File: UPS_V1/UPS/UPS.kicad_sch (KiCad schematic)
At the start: 77 parts, among them J1 Conn_01x02_Pin, J2 Conn_01x02_Pin, J3 USB_B_Micro, J4 Conn_01x02_Socket, J5 Conn_01x02_Pin, J6 Conn_01x02_Socket, U1 MT3608, U2 BQ24040DSQR, U3 LM2903, U4 TPS22810DRV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

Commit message: pcb layout
minor schematic adjustment and pcb layout
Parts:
- removed unit 2 of U3
- added H1, H2, H3, H4: MountingHole, MountingHole:MountingHole_3.2mm_M3, symbol Mechanical:MountingHole
- added J7: Conn_01x02_Pin, Connector_PinHeader_2.54mm:PinHeader_1x02_P2.54mm_Vertical, symbol Connector:Conn_01x02_Pin
- added J8, J9: Screw_Terminal_01x02, TerminalBlock:TerminalBlock_Xinya_XY308-2.54-2P_1x02_P2.54mm_Horizontal, symbol Connector:Screw_Terminal_01x02
- J1: footprint (none) -> Connector_PinHeader_2.54mm:PinHeader_1x02_P2.54mm_Vertical
- RV1: footprint footprints:3296W-1-103_BRN -> 3296W:3296W-1-103_BRN
- U2: footprint DSQ10_P9X1P5 -> BQ24040DSQR:DSQ10_P9X1P5
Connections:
- net 3.3VOUT: now also J8.1 (Pin_1)
- net 5VOUT: now also J9.1 (Pin_1)
- net GND: now also J7.1 (Pin_1), J8.2 (Pin_2), J9.2 (Pin_2)
- net at R8.2, U3.1, U4.5 (EN/UVLO): now also J7.2 (Pin_2)
- no-connect marks 6 -> 3

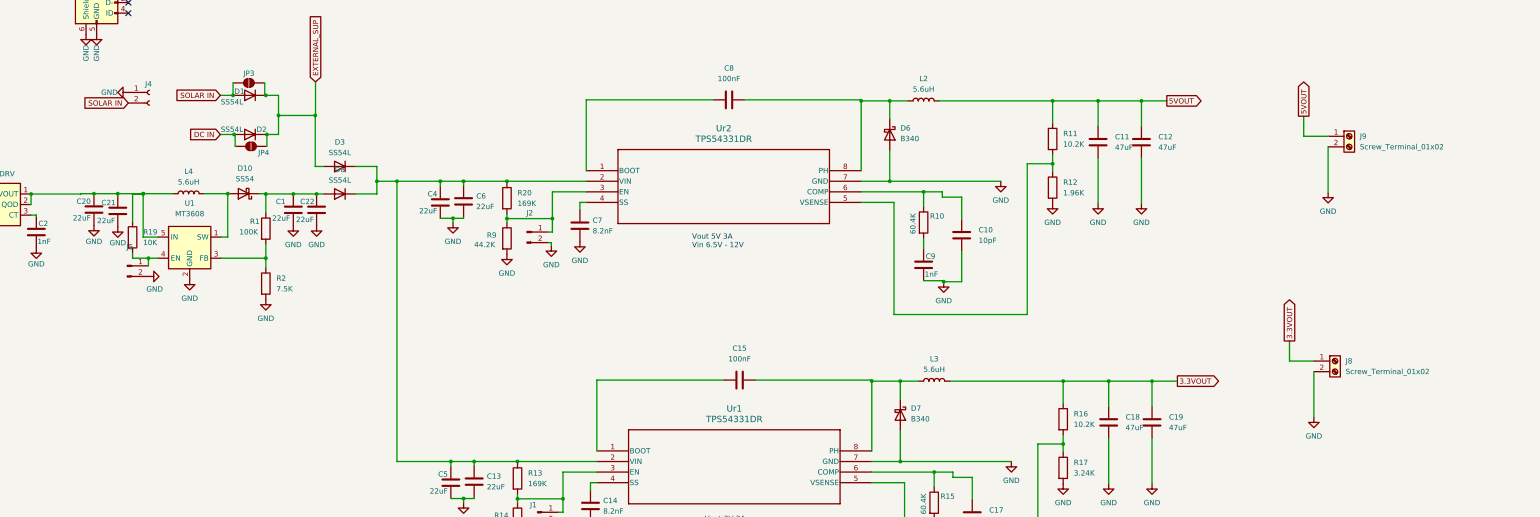
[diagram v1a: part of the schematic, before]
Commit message: added 1x12 terminal block
 1x12 terminal block
3d
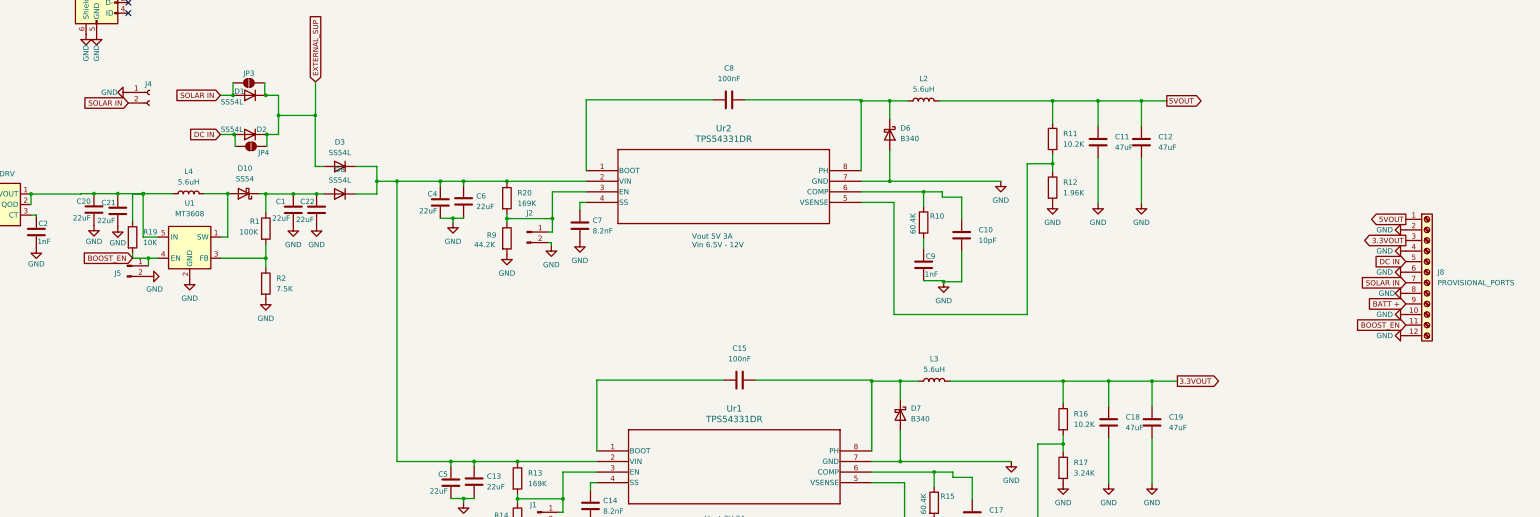
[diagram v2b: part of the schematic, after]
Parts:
- removed J8, J9: Screw_Terminal_01x02, TerminalBlock:TerminalBlock_Xinya_XY308-2.54-2P_1x02_P2.54mm_Horizontal, symbol Connector:Screw_Terminal_01x02
- added J8: PROVISIONAL_PORTS, TerminalBlock:TerminalBlock_Xinya_XY308-2.54-12P_1x12_P2.54mm_Horizontal, symbol Connector:Screw_Terminal_01x12
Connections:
- net 3.3VOUT: now also J8.3 (Pin_3)
- net 5VOUT: now also J8.1 (Pin_1)
- net BATT +: now also J8.9 (Pin_9)
- net DC IN: now also J8.5 (Pin_5)
- net GND: now also J8.10 (Pin_10), J8.12 (Pin_12), J8.2 (Pin_2), J8.4 (Pin_4), J8.6 (Pin_6), J8.8 (Pin_8)
- net SOLAR IN: now also J8.7 (Pin_7)
- net BOOST_EN: now reaches J5.1 (Pin_1), R19.2, U1.4 (EN)
- net BOOST_EN: now also J8.11 (Pin_11)

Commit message: -
updated symbol and footprint
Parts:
- C15, C8: footprint Capacitor_SMD:C_0201_0603Metric_Pad0.64x0.40mm_HandSolder -> Capacitor_SMD:C_0603_1608Metric_Pad1.08x0.95mm_HandSolder
- U4: value TPS22810DRV -> TPS22810DBVR; footprint Package_SON:WSON-6-1EP_2x2mm_P0.65mm_EP1x1.6mm -> InnovationCentral:SOT-23-6_L2.9-W1.6-P0.95-LS2.8-BL; symbol Power_Management:TPS22810DRV -> 2024-09-10_13-19-56:TPS22810DBVR
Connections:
- net BATT +: now also U4.1 (VIN); no longer U4.6 (VIN)
- net GND: now also U4.2 (GND); no longer U4.4 (GND), U4.7 (GND)
- net at C20.1, C21.1, L4.1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: now also U4.5 (QOD), U4.6 (VOUT); no longer U4.1 (VOUT), U4.2 (QOD)
- net at U4.3 (EN/UVLO): now also J7.2 (Pin_2), R8.2, U3.1; no longer C2.2
- new net: C2.2, U4.4 (CT)
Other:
- moved on the sheet: C2, R8, U4
